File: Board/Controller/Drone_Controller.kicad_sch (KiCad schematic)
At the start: 14 parts, among them U1 NUCLEO144-H743ZI, U2 BMP581, U3 VL53L1CBV0FY-1, U4 AT30TS74-XM8M-T, U5 LSM6DSOTR

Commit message: added connector
Signed-off-by: EricTheGreat <joesmith01110000011101010111@gmail.com>
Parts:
- added J?: 140-506-415-000, KiCad_Cust:140-506-415-000, symbol KiCad_Cust:140-506-415-000
- gave numbers to parts that had none: 7
- renumbered U5 to U4, U4 to U5
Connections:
- net SPI2_MISO: now also U1.35 (PC2)
- net SPI2_MOSI: now also U1.98 (PB15)
- net SPI2_NSS: now also U1.88 (PB12)
- net SPI2_SCK: now also U1.97 (PB10)
- net LIDAR_EXT: now reaches R3.2, U3.7 (GPIO1)
- net I2C1_SCL: now reaches R2.2, U3.10 (SCL)
- net I2C1_SCL: now also U1.89 (PB6)
- net I2C1_SDA: now reaches R1.2, U3.9 (SDA)
- net I2C1_SDA: now also U1.21 (LD2/PB7)

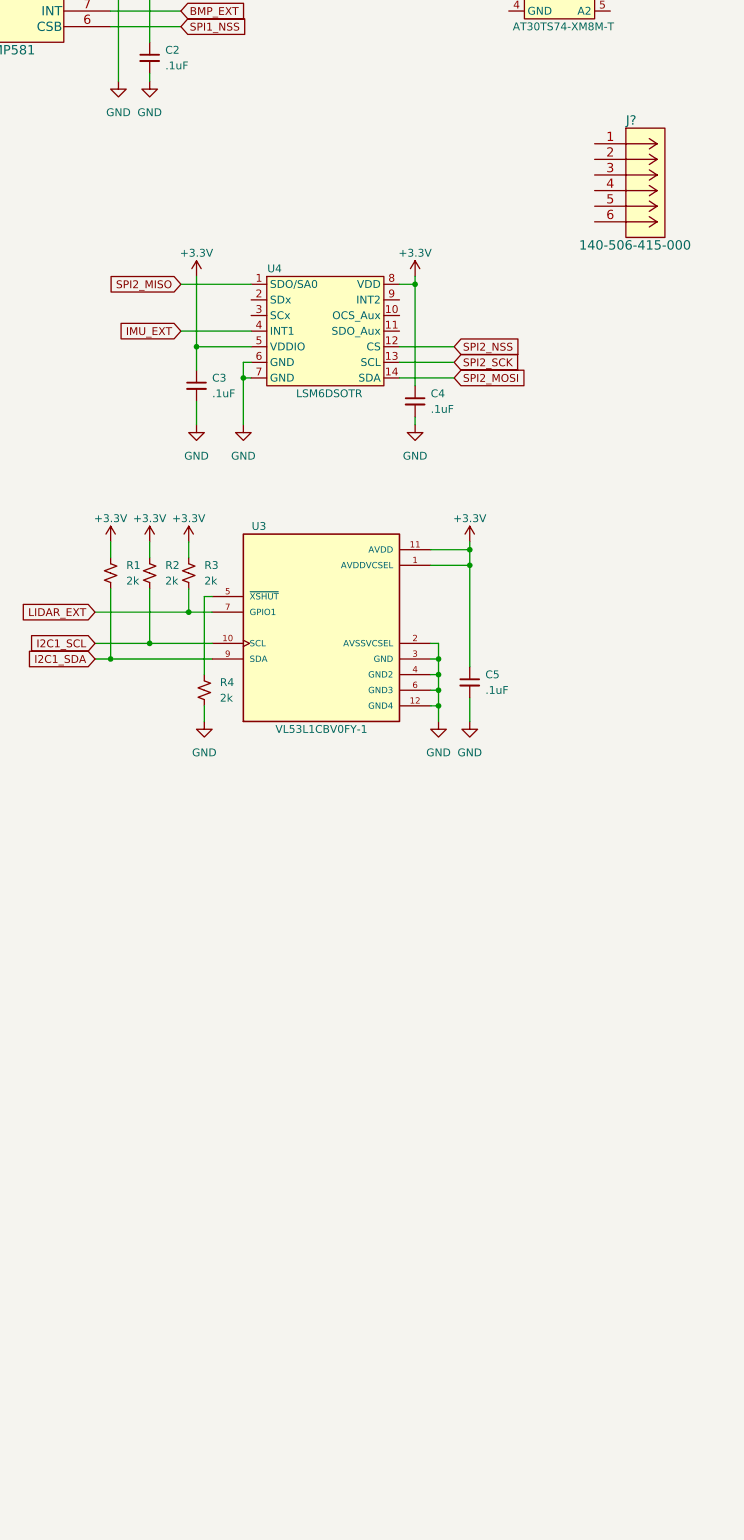
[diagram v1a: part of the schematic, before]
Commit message: added top load connector
Signed-off-by: EricTheGreat <joesmith01110000011101010111@gmail.com>
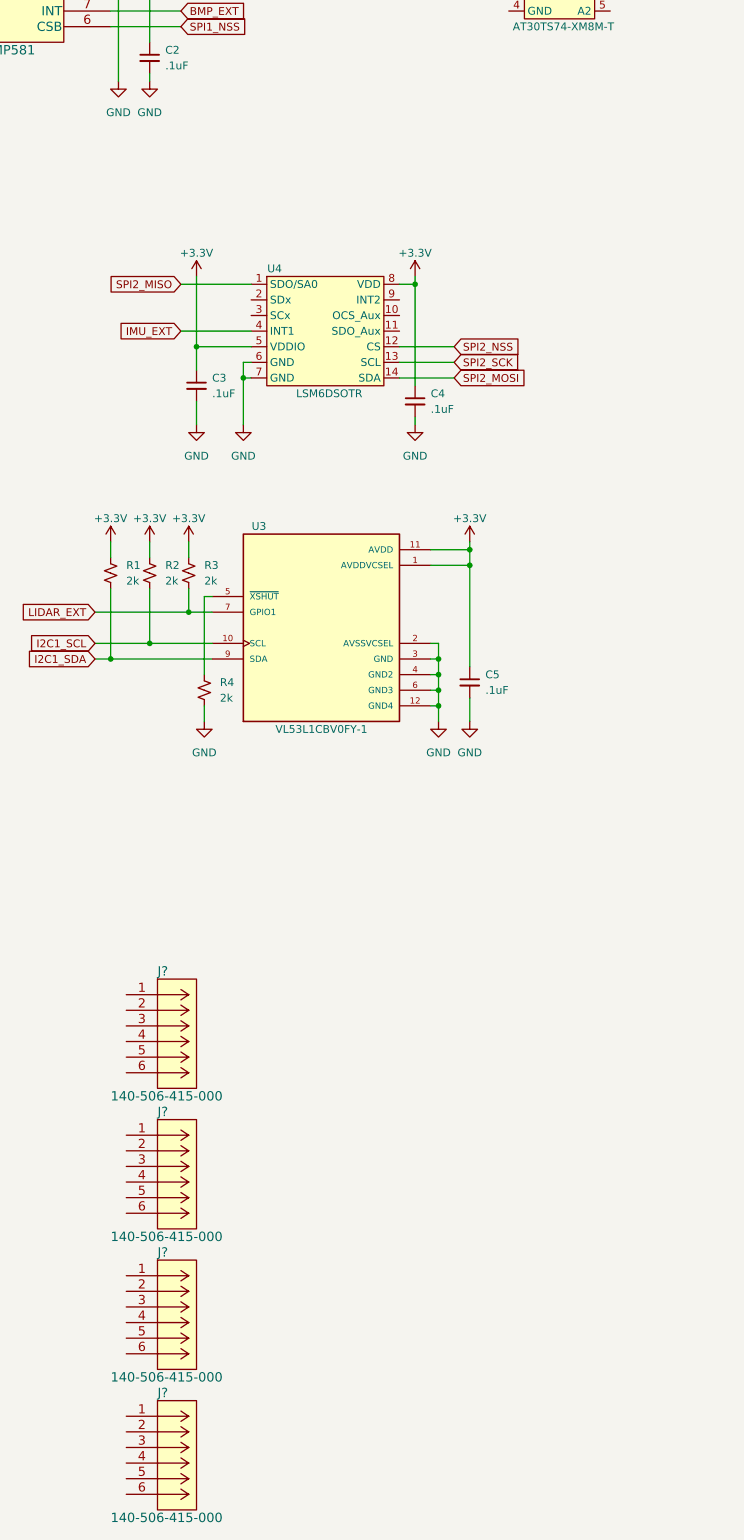
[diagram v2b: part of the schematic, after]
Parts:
- added J? (x3): 140-506-415-000, KiCad_Cust:140-506-415-000, symbol KiCad_Cust:140-506-415-000
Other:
- moved on the sheet: J?
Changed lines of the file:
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@@
     (pin "1")
+  )
+  (symbol (lib_id "KiCad_Cust:140-506-415-000") (at 179.07 260.35 0) (unit 1)
+    (in_bom yes) (on_board yes)
+    (property "Reference" "J?" (id 0) (at 184.15 256.54 0)
+      (effects (font (size 1.524 1.524)) (justify left))
+    )
+    (property "Value" "140-506-415-000" (id 1) (at 176.53 276.86 0)
+      (effects (font (size 1.524 1.524)) (justify left))
+    )
+    (property "Footprint" "KiCad_Cust:140-506-415-000" (id 2) (at 189.23 266.954 0)
+      (effects (font (size 1.524 1.524)) hide)
+    )
+    (property "Datasheet" "https://files.edac.net/edac/content/series/og/English/EDAC%20140%20Series%20Standard%20(non%20WP)%20W-WW-B%20English%20Ordering%20Guide.pdf" (id 3) (at 179.07 260.35 0)
+      (effects (font (size 1.524 1.524)) hide)
+    )
+    (property "Mates with" "140-506-210-011" (id 4) (at 179.07 260.35 0)
+      (effects (font (size 1.27 1.27)) hide)
+    )
+    (property "Crimp Connectors" "140-941-290" (id 5) (at 179.07 260.35 0)
+      (effects (font (size 1.27 1.27)) hide)
+    )
+    (pin "1")
+    (pin "2")
+    (pin "3")
+    (pin "4")
+    (pin "5")
+    (pin "6")
   )
   (symbol (lib_id "power:GND") (at 134.62 66.04 0) (unit 1)
@@
     (pin "1")
   )
-  (symbol (lib_id "KiCad_Cust:140-506-415-000") (at 255.27 76.2 0) (unit 1)
-    (in_bom yes) (on_board yes)
-    (property "Reference" "J?" (id 0) (at 260.35 72.39 0)
+  (symbol (lib_id "KiCad_Cust:140-506-415-000") (at 179.07 214.63 0) (unit 1)
+    (in_bom yes) (on_board yes)
+    (property "Reference" "J?" (id 0) (at 184.15 210.82 0)
       (effects (font (size 1.524 1.524)) (justify left))
     )
-    (property "Value" "140-506-415-000" (id 1) (at 252.73 92.71 0)
+    (property "Value" "140-506-415-000" (id 1) (at 176.53 231.14 0)
       (effects (font (size 1.524 1.524)) (justify left))
     )
-    (property "Footprint" "KiCad_Cust:140-506-415-000" (id 2) (at 265.43 82.804 0)
-      (effects (font (size 1.524 1.524)) hide)
-    )
-    (property "Datasheet" "https://files.edac.net/edac/content/series/og/English/EDAC%20140%20Series%20Standard%20(non%20WP)%20W-WW-B%20English%20Ordering%20Guide.pdf" (id 3) (at 255.27 76.2 0)
-      (effects (font (size 1.524 1.524)) hide)
-    )
-    (property "Mates with" "140-506-210-011" (id 4) (at 255.27 76.2 0)
-      (effects (font (size 1.27 1.27)) hide)
-    )
-    (property "Crimp Connectors" "140-941-290" (id 5) (at 255.27 76.2 0)
+    (property "Footprint" "KiCad_Cust:140-506-415-000" (id 2) (at 189.23 221.234 0)
+      (effects (font (size 1.524 1.524)) hide)
+    )
+    (property "Datasheet" "https://files.edac.net/edac/content/series/og/English/EDAC%20140%20Series%20Standard%20(non%20WP)%20W-WW-B%20English%20Ordering%20Guide.pdf" (id 3) (at 179.07 214.63 0)
+      (effects (font (size 1.524 1.524)) hide)
+    )
+    (property "Mates with" "140-506-210-011" (id 4) (at 179.07 214.63 0)
+      (effects (font (size 1.27 1.27)) hide)
+    )
+    (property "Crimp Connectors" "140-941-290" (id 5) (at 179.07 214.63 0)
       (effects (font (size 1.27 1.27)) hide)
     )
@@
     (pin "1")
   )
+  (symbol (lib_id "KiCad_Cust:140-506-415-000") (at 179.07 237.49 0) (unit 1)
+    (in_bom yes) (on_board yes)
+    (property "Reference" "J?" (id 0) (at 184.15 233.68 0)
+      (effects (font (size 1.524 1.524)) (justify left))
+    )
+    (property "Value" "140-506-415-000" (id 1) (at 176.53 254 0)
+      (effects (font (size 1.524 1.524)) (justify left))
+    )
+    (property "Footprint" "KiCad_Cust:140-506-415-000" (id 2) (at 189.23 244.094 0)
+      (effects (font (size 1.524 1.524)) hide)
+    )
+    (property "Datasheet" "https://files.edac.net/edac/content/series/og/English/EDAC%20140%20Series%20Standard%20(non%20WP)%20W-WW-B%20English%20Ordering%20Guide.pdf" (id 3) (at 179.07 237.49 0)
+      (effects (font (size 1.524 1.524)) hide)
+    )
+    (property "Mates with" "140-506-210-011" (id 4) (at 179.07 237.49 0)
+      (effects (font (size 1.27 1.27)) hide)
+    )
+    (property "Crimp Connectors" "140-941-290" (id 5) (at 179.07 237.49 0)
+      (effects (font (size 1.27 1.27)) hide)
+    )
+    (pin "1")
+    (pin "2")
+    (pin "3")
+    (pin "4")
+    (pin "5")
+    (pin "6")
+  )
   (symbol (lib_id "Device:C_Small") (at 134.62 62.23 0) (unit 1)
     (in_bom yes) (on_board yes) (fields_autoplaced)
@@
     )
     (pin "1")
+  )
+  (symbol (lib_id "KiCad_Cust:140-506-415-000") (at 179.07 283.21 0) (unit 1)
+    (in_bom yes) (on_board yes)
+    (property "Reference" "J?" (id 0) (at 184.15 279.4 0)
+      (effects (font (size 1.524 1.524)) (justify left))
+    )
+    (property "Value" "140-506-415-000" (id 1) (at 176.53 299.72 0)
+      (effects (font (size 1.524 1.524)) (justify left))
+    )
+    (property "Footprint" "KiCad_Cust:140-506-415-000" (id 2) (at 189.23 289.814 0)
+      (effects (font (size 1.524 1.524)) hide)
+    )
+    (property "Datasheet" "https://files.edac.net/edac/content/series/og/English/EDAC%20140%20Series%20Standard%20(non%20WP)%20W-WW-B%20English%20Ordering%20Guide.pdf" (id 3) (at 179.07 283.21 0)
+      (effects (font (size 1.524 1.524)) hide)
+    )
+    (property "Mates with" "140-506-210-011" (id 4) (at 179.07 283.21 0)
+      (effects (font (size 1.27 1.27)) hide)
+    )
+    (property "Crimp Connectors" "140-941-290" (id 5) (at 179.07 283.21 0)
+      (effects (font (size 1.27 1.27)) hide)
+    )
+    (pin "1")
+    (pin "2")
+    (pin "3")
+    (pin "4")
+    (pin "5")
+    (pin "6")
   )
   (symbol (lib_id "KiCad_Cust:AT30TS74-XM8M-T") (at 250.19 50.8 0) (unit 1)
@@
       (reference "C5") (unit 1) (value ".1uF") (footprint "Resistor_SMD:R_0805_2012Metric")
     )
+    (path "/4bf9b909-471b-4417-abda-1bac1efb2adc"
+      (reference "J?") (unit 1) (value "140-506-415-000") (footprint "KiCad_Cust:140-506-415-000")
+    )
     (path "/4f86d78a-c15c-4987-91d8-81e1560eb131"
       (reference "J?") (unit 1) (value "140-506-415-000") (footprint "KiCad_Cust:140-506-415-000")
     )
+    (path "/a83c5b21-cadb-4730-af6f-68b5b15dd36c"
+      (reference "J?") (unit 1) (value "140-506-415-000") (footprint "KiCad_Cust:140-506-415-000")
+    )
+    (path "/c8caf12c-788c-4457-ab8a-0644ce663cb0"
+      (reference "J?") (unit 1) (value "140-506-415-000") (footprint "KiCad_Cust:140-506-415-000")
+    )

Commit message: added battery mux and LIDAR connectors
Signed-off-by: EricTheGreat <joesmith01110000011101010111@gmail.com>
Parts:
- removed J? (x3): 140-506-415-000, KiCad_Cust:140-506-415-000, symbol KiCad_Cust:140-506-415-000
- removed U5: AT30TS74-XM8M-T, Package_SO:MSOP-8_3x3mm_P0.65mm, symbol KiCad_Cust:AT30TS74-XM8M-T
- added J2, J3, J4, J5, J6: 140-506-415-000, KiCad_Cust:140-506-415-000, symbol KiCad_Cust:140-506-415-000
- added R10, R11, R12, R13, R14, R15, R16, R5, R6, R7, R8, R9: 2k, Resistor_SMD:R_0805_2012Metric, symbol Device:R_Small_US
- added R17, R20, R23, R25, R26, R29, R32, R35, R38, R41, R44, R47, R50, R51, R52, R53: 1Meg, Resistor_SMD:R_0805_2012Metric, symbol Device:R_Small_US
- added R18: 68k, Resistor_SMD:R_0805_2012Metric, symbol Device:R_Small_US
- added R19: 4.7k, Resistor_SMD:R_0805_2012Metric, symbol Device:R_Small_US
- added R21, R34: 47k, Resistor_SMD:R_0805_2012Metric, symbol Device:R_Small_US
- added R22: 33k, Resistor_SMD:R_0805_2012Metric, symbol Device:R_Small_US
- added R24, R27, R30, R33, R39, R40: 100k, Resistor_SMD:R_0805_2012Metric, symbol Device:R_Small_US
- added R28, R46: 3.3k, Resistor_SMD:R_0805_2012Metric, symbol Device:R_Small_US
- added R31: 22k, Resistor_SMD:R_0805_2012Metric, symbol Device:R_Small_US
- added R36: 150k, Resistor_SMD:R_0805_2012Metric, symbol Device:R_Small_US
- added R37: 6.8k, Resistor_SMD:R_0805_2012Metric, symbol Device:R_Small_US
- added R42: 470k, Resistor_SMD:R_0805_2012Metric, symbol Device:R_Small_US
- added R43: 680k, Resistor_SMD:R_0805_2012Metric, symbol Device:R_Small_US
- added R45: 300k, Resistor_SMD:R_0805_2012Metric, symbol Device:R_Small_US
- added R48: 270k, Resistor_SMD:R_0805_2012Metric, symbol Device:R_Small_US
- added R49: 330k, Resistor_SMD:R_0805_2012Metric, symbol Device:R_Small_US
- added U5: CD74HC4067M, Package_SO:SOIC-24W_7.5x15.4mm_P1.27mm, symbol 74xx:CD74HC4067M
- gave numbers to parts that had none: 1
- renumbered U2 to U1, U1 to U2
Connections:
- net +3V3: now also J1.6, R4.2, J2.6, J3.6, J4.6, R10.1, R11.1, R12.1, R13.1, R14.1, R15.1, R16.1, R5.1, R6.1, R7.1, R8.1, R9.1, U5.24 (VCC)
- net GND: now also J1.1, J1.2, J2.1, J2.2, J3.1, J3.2, J4.1, J4.2, R19.2, R22.2, R24.2, R25.2, R28.2, R31.2, R34.2, R37.2, R40.2, R42.2, R43.2, R46.2, R49.2, R53.2, U5.12 (GND); no longer R4.2
- net I2C2_SCL: now reaches J1.3
- net I2C2_SCL: now also U2.51 (PF1), R5.2, R9.2
- net I2C2_SDA: now reaches J1.4
- net I2C2_SDA: now also U2.90 (PB11)
- net LIDAR2_EXT: now reaches J1.5
- net LIDAR2_EXT: now also R13.2
- net I2C4_SCL: now reaches U2.122 (PF14)
- net I2C4_SCL: now also J3.3, R11.2, R7.2
- net I2C4_SDA: now reaches U2.132 (PF15)
- net I2C4_SDA: now also J3.4
- net I2C5_SCL: now reaches U2.2 (PC11)
- net I2C5_SCL: now also J4.3, R12.2, R8.2
- net I2C5_SDA: now reaches U2.53 (PF0)
- net I2C5_SDA: now also J4.4
- net I2C3_SDA: now reaches U2.73 (PC9)
- net I2C3_SDA: now also J2.4
- net I2C3_SCL: now reaches U2.95 (USB_SOF/PA8)
- net I2C3_SCL: now also J2.3, R10.2, R6.2
- net LIDAR_EXT renamed LIDAR1_EXT
- new net: R45.2, R46.1
- new net: J6.2, R47.1
- new net: R33.2, R34.1
- new net: J6.4, R41.1
- new net: J5.5, R20.1
- new net: J5.1, R32.1
- new net: R27.2, R28.1
- new net: R51.2, R52.1
- new net: R52.2, R53.1
- new net: J5.3, R26.1
- new net: R30.2, R31.1
- new net: J5.2, R29.1
- new net: J5.4, R23.1
- new net: J5.6, R17.1
- new net: R36.2, R37.1
- new net: R21.2, R22.1
- new net: J6.1, R50.1
- new net: R48.2, R49.1
- new net: R39.2, R40.1
- new net: J6.6, R35.1
- new net: J6.5, R38.1
- new net: R18.2, R19.1
- new net: J6.3, R44.1
- new net LIDAR3_EXT: J2.5, R14.2
- new net LIDAR4_EXT: J3.5, R15.2
- new net LIDAR5_EXT: J4.5, R16.2
- new net S0: U5.10 (S0)
- new net S1: U5.11 (S1)
- new net S2: U5.14 (S2)
- new net S3: U5.13 (S3)
- new net V12: R44.2, R45.1, U5.22 (I9)
- new net V14: R41.2, R42.1, R43.1, U5.23 (I8)
- new net V18: R38.2, R39.1, U5.2 (I7)
- new net V22: R35.2, R36.1, U5.3 (I6)
- new net V24: R32.2, R33.1, U5.4 (I5)
- new net V28: R29.2, R30.1, U5.5 (I4)
- new net V32: R26.2, R27.1, U5.6 (I3)
- new net V36: R23.2, R24.1, R25.1, U5.7 (I2)
- new net V4: R50.2, R51.1, U5.20 (I11)
- new net V40: R20.2, R21.1, U5.8 (I1)
- new net V44: R17.2, R18.1, U5.9 (I0)
- new net V8: R47.2, R48.1, U5.21 (I10)
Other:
- moved on the sheet: J1, U2
